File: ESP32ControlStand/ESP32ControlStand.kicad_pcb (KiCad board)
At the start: 2 copper layers, 184.1 x 144.8 mm, 116 parts, among them CON101 BARREL_JACK, J101 Button & LED Panel, J102 Horn, J103 Brake, J104 I2C Display, J105 Button & LED Panel, J106 Light Switch, J107 Reverser, J108 Throttle, J401 RJ45, J402 RJ45, P101 CONN_8, P102 Misc buttons, bell, status LED, P106 CONN_3, P107 CONN_3, P201 CONN_5, P301 CONN_5, SW101 A, SW102 B, SW103 C, SW104 D, SW105 Bell, SW201 SW_PUSH_SMALL, SW202 SW_PUSH_SMALL, SW203 SW_PUSH_SMALL, SW204 SW_PUSH_SMALL, SW205 SW_PUSH_SMALL, SW206 SW_PUSH_SMALL, SW207 SW_PUSH_SMALL, SW208 SW_PUSH_SMALL, SW301 SW_PUSH_SMALL, SW302 SW_PUSH_SMALL, SW303 SW_PUSH_SMALL, SW304 SW_PUSH_SMALL, SW305 SW_PUSH_SMALL, SW306 SW_PUSH_SMALL, SW307 SW_PUSH_SMALL, SW308 SW_PUSH_SMALL, T201 Buttons, T202 LEDS, T301 Buttons, T302 LEDS, T401 + 15 in -, T402 + 15 out -, U101 ADAFRUIT_POWERBOOST_500, U102 TTGO-T1, U201 MCP23017, U202 TBD62083A, U301 MCP23017, U302 TBD62083A, U401 TCAN332DR, U402 SN65HVD233-HT, U501 LM2574N-5.0

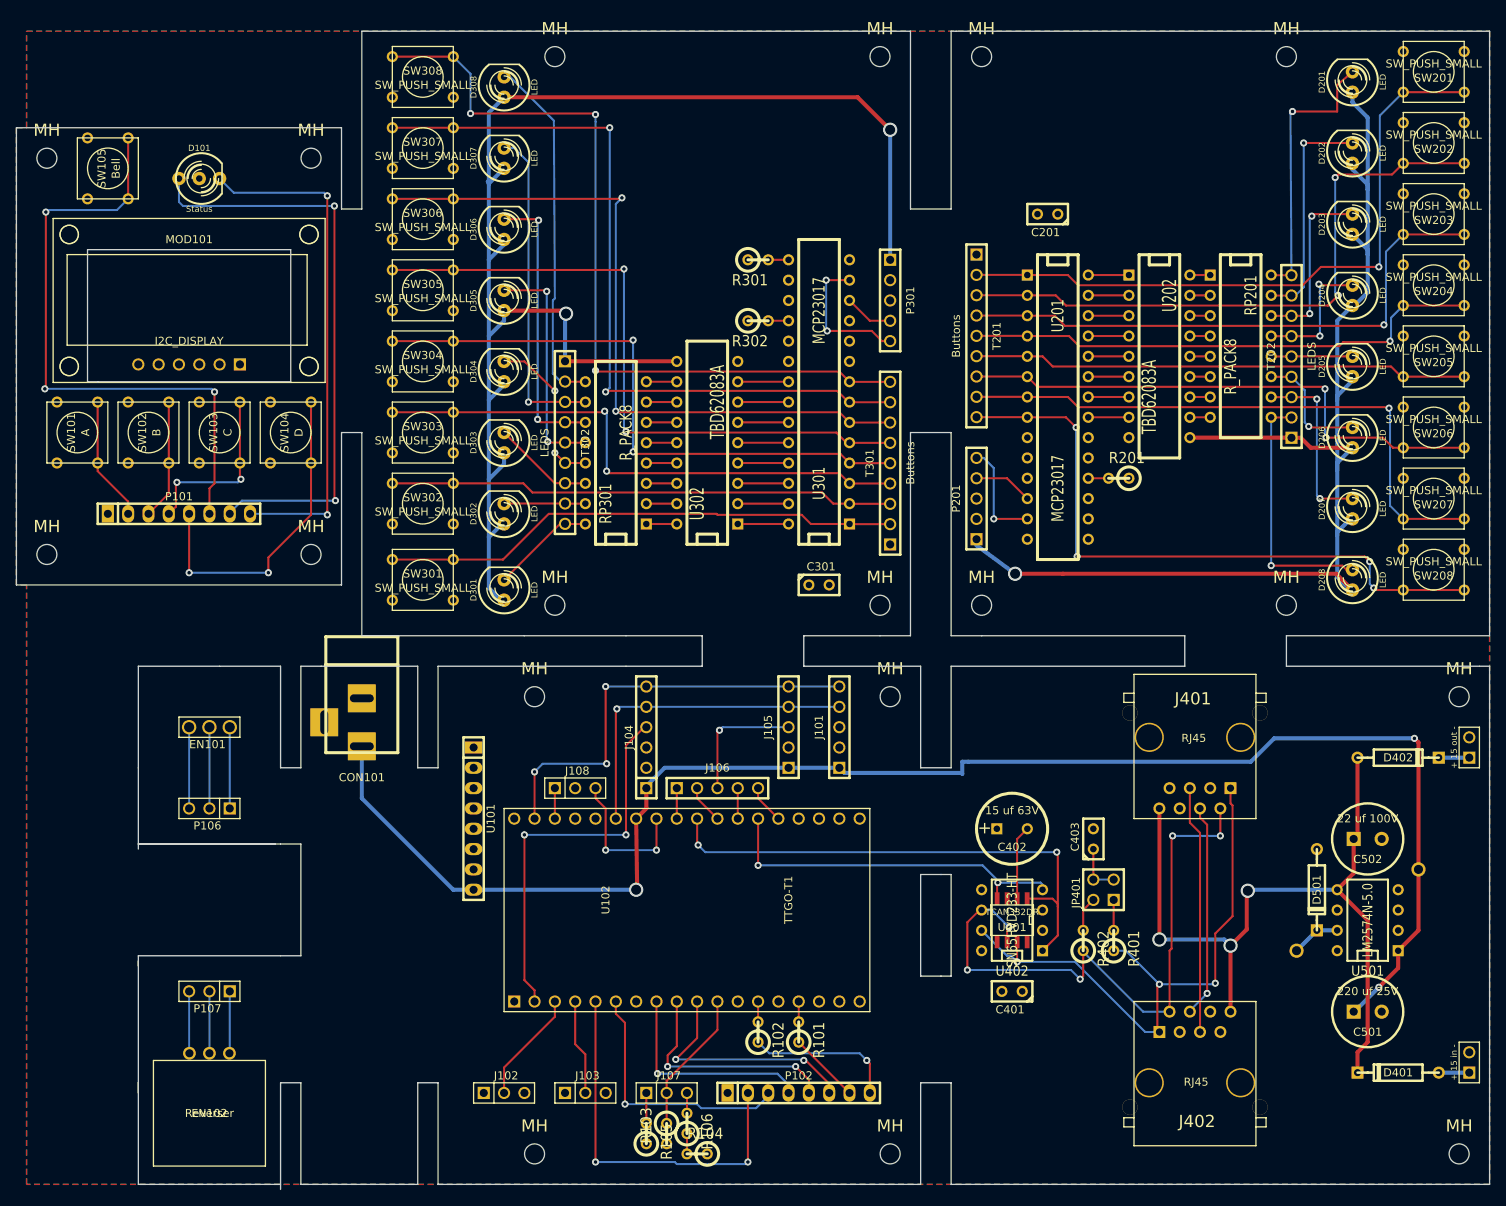
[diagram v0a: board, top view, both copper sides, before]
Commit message: Tweaks of PCBs for ESP32ControlStand.
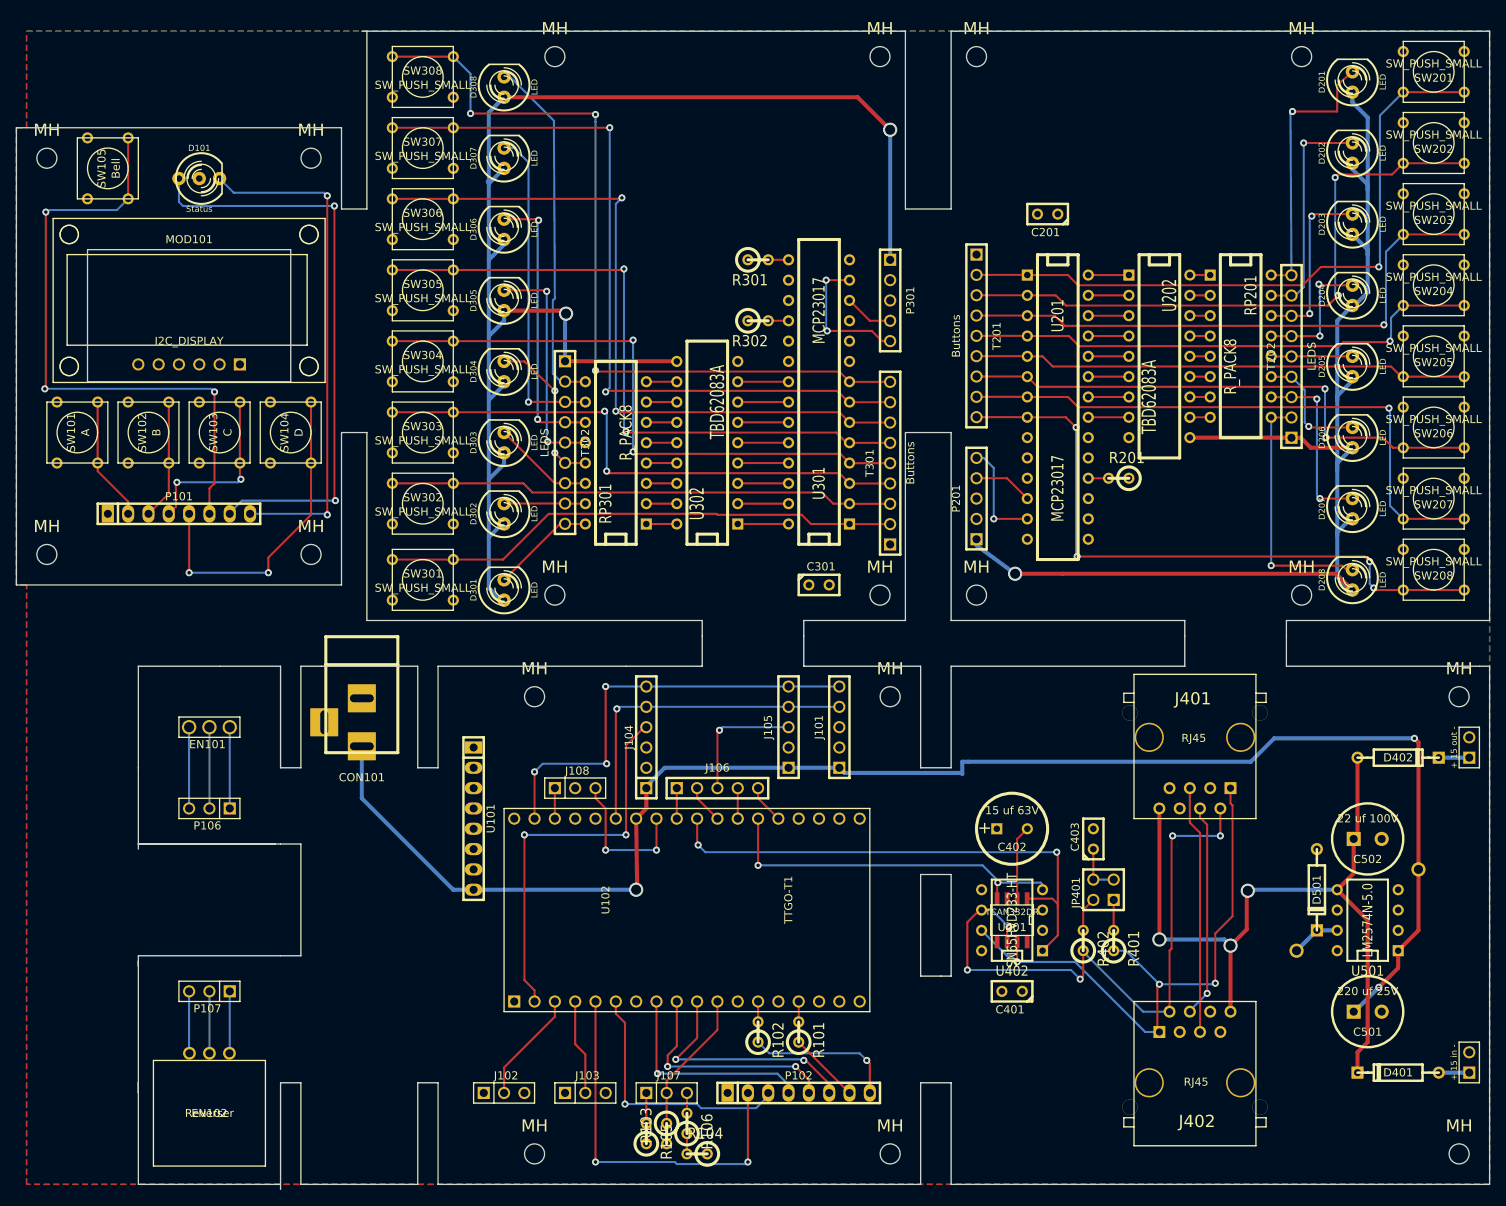
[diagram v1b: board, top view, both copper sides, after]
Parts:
- moved MH 2.29 mm to (275.0, 156.2)
- moved MH 1.90 mm to (275.0, 88.9)
- moved MH 1.42 mm to (234.3, 156.2)
- moved MH 1.27 mm to (181.6, 156.2)
- moved MH 1.27 mm to (222.2, 156.2)
- moved MH 0.63 mm to (234.3, 88.9)
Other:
- outline, holes or cut-outs redrawn

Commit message: Assorted updates to the PCB.
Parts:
- added J109: On-Off Switch, PIN_ARRAY_2X1, F.Cu at (175.3, 179.1)
- EN101: footprint Bourns_ECW -> Series25L-Encoder
- moved EN101 6.63 mm to (132.1, 170.8), turned to 0 degrees
- moved P106 6.48 mm to (132.1, 184.2), turned to 0 degrees
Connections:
- U101 pad 4: (no net) -> N-0000039
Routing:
- net N-0000039: track 0.00 -> 4.86 mm
- net N-0000060: track 10.2 -> 5.72 mm
- net N-0000059: track 10.2 -> 5.72 mm
- net N-0000058: track 10.2 -> 5.72 mm
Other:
- outline, holes or cut-outs redrawn

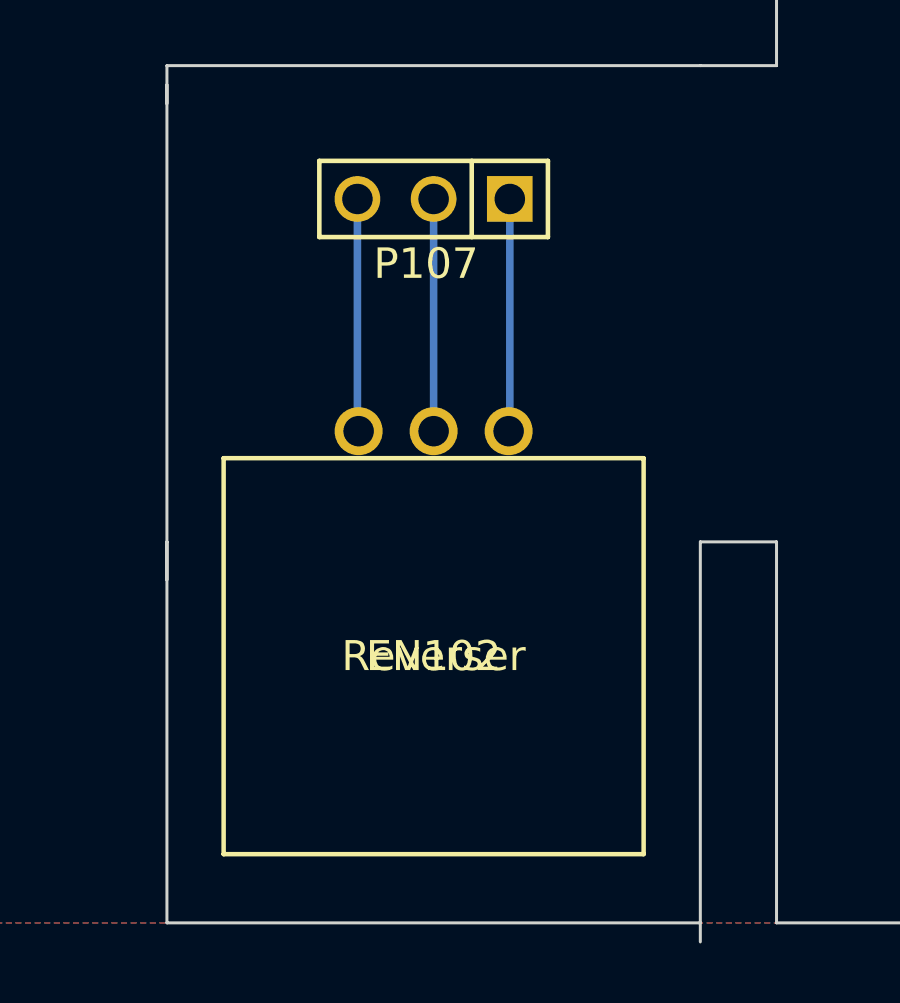
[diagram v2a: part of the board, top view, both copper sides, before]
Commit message: Continue 3D model, spec out horn and brake pots, noturn hole for reverser.
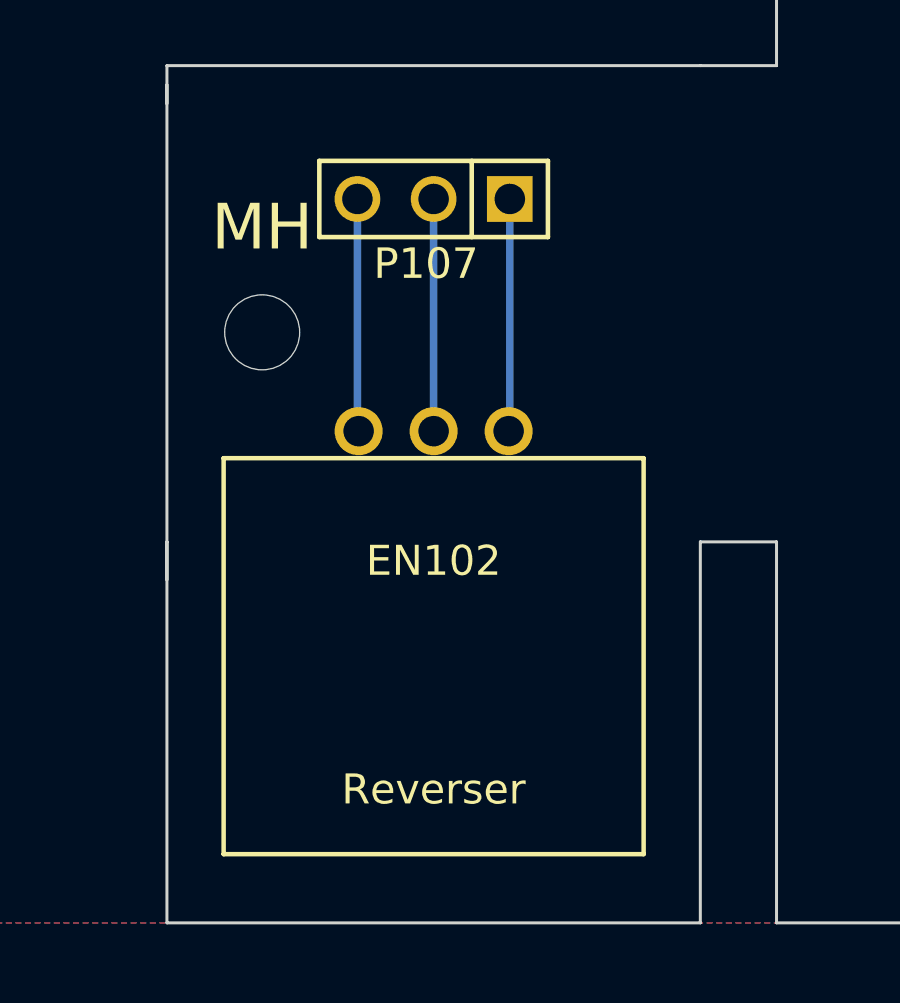
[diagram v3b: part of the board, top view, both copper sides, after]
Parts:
- added MH: MountingHole_2-5mm_RevA_Date21Jun2010, MountingHole_2-5mm_RevA_Date21Jun2010, F.Cu at (132.7, 210.2)
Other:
- board size 184.1 x 144.8 mm -> 184.1 x 144.1 mm
